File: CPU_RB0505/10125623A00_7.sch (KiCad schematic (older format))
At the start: 71 parts, among them IC20 SN74LVC1G07DBVT, IC6 SN74LVC1G07DBVT, J1 ZIF-52610-2290, J17 FH_40BR, J3 , J6 87606-408, J7 26BR-HE10, T1 2N7002, T16 IRLML5103, T2 2N7002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

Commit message: Renumbered J1's symbol to match footprint
And updated PCB from schematic
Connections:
- wire segments 350 -> 371
- no-connect marks 46 -> 25

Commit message: fix erc errors, change many pin electrical types
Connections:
- wire segments 371 -> 372
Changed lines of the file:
@@
 Text HLabel 8400 4350 0    50   Output ~ 0
 RX-UART-ST
-Text Label 8400 4550 2    50   ~ 0
-LED-PRESENCE-DC
 Text Label 3225 5025 0    56   ~ 0
 LED-PRESENCE-DC
@@
 U 1 1 7D94D0D3
 P 2275 10075
+AR Path="/7D94D0D3" Ref="J3"  Part="1"
+AR Path="/5E926050/7D94D0D3" Ref="J3"  Part="1"
 F 0 "J3" H 2200 9975 59  0000 L BNN
 F 1 " " H 2200 9887 59  0000 L BNN
@@
 	6450 10325 6750 10325
 Wire Wire Line
-	7350 9875 7350 9550
+	7350 9875 7350 9700
 Wire Wire Line
 	7050 9800 7050 9875
@@
 Wire Wire Line
 	2800 5625 3000 5625
-Wire Bus Line
-	12600 2775 14225 2775
-Wire Bus Line
-	11400 3025 14200 3025
 Connection ~ 3000 2025
 Connection ~ 3000 2225
@@
 Connection ~ 3000 5625
 Connection ~ 3000 5825
+$Comp
+L power:PWR_FLAG #FLG0102
+U 1 1 5EB97020
+P 15050 4150
+F 0 "#FLG0102" H 15050 4225 50  0001 C CNN
+F 1 "PWR_FLAG" V 15050 4278 50  0000 L CNN
+F 2 "" H 15050 4150 50  0001 C CNN
+F 3 "~" H 15050 4150 50  0001 C CNN
+	1    15050 4150
+	0    1    1    0
+$EndComp
+Connection ~ 15050 4150
+Text Label 8400 4550 2    50   ~ 0
+LED-PRESENCE-DC
+Wire Bus Line
+	12600 2775 14225 2775
+Wire Bus Line
+	11400 3025 14200 3025
+$Comp
+L power:PWR_FLAG #FLG0110
+U 1 1 600678A7
+P 7325 7475
+F 0 "#FLG0110" H 7325 7550 50  0001 C CNN
+F 1 "PWR_FLAG" V 7325 7603 50  0000 L CNN
+F 2 "" H 7325 7475 50  0001 C CNN
+F 3 "~" H 7325 7475 50  0001 C CNN
+	1    7325 7475
+	0    1    1    0
+$EndComp
+Connection ~ 7325 7475
+$Comp
+L power:PWR_FLAG #FLG0111
+U 1 1 60083738
+P 7350 9700
+F 0 "#FLG0111" H 7350 9775 50  0001 C CNN
+F 1 "PWR_FLAG" V 7350 9828 50  0000 L CNN
+F 2 "" H 7350 9700 50  0001 C CNN
+F 3 "~" H 7350 9700 50  0001 C CNN
+	1    7350 9700
+	0    1    1    0
+$EndComp
+Connection ~ 7350 9700
+Wire Wire Line
+	7350 9700 7350 9550
 $EndSCHEMATC

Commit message: CPU schematic updated to Kicad resistor and cap symbols
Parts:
- C19, C31, C32, C34: symbol cpu-board:TANTALB -> Flipped_Devices:CP_Small
- C35: symbol cpu-board:C0805 -> Flipped_Devices:C_Small
- C87: symbol cpu-board:C0603 -> Flipped_Devices:C_Small
- L5, R12, R13, R20, R21, R24, R25, R26, R27, R30, R32, R47, R7: symbol cpu-board:R0805 -> Flipped_Devices:R
- R16, R22, R23, R31: symbol cpu-board:R1206 -> Flipped_Devices:R
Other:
- moved on the sheet: C17, C18, C41, C52, C55, IC20, IC6, J1, J3, J6, J7, JP1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

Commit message: CPU board diode and transistor symbols changed to Kicad symbols
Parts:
- L1, L16, L18, L3, L35, L36, L38, L39, L4, L40, L41, L42, L43, L44, L45, L46, L47, L48, L49, L50, L51, L52, L53, L6: symbol cpu-board:74279263 -> Flipped_Devices:L
- L61, L8: symbol cpu-board:7427504 -> Flipped_Devices:L
- T1, T2, T4, T5: symbol cpu-board:IRLML2803 -> Flipped_Devices:Q_NMOS_GSD
- T16: symbol cpu-board:IRLML5103 -> Flipped_Devices:Q_PMOS_GSD
- T8, T9: symbol cpu-board:IRLML2803@2 -> Flipped_Devices:Q_NMOS_GSD

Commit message: ran renameSchSyms.py
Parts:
- C19: symbol Flipped_Devices:CP_Small -> Capacitor:C_47uF_10V_10%
- C31, C32, C34: symbol Flipped_Devices:CP_Small -> Capacitor:C_1uF_35V_10%
- C87: symbol Flipped_Devices:C_Small -> Capacitor:C0402_100nF_16V_10%
- IC20: symbol cpu-board:LVC1G07DBVT -> IC:LVC1G07DBVT
- J1: symbol cpu-board:ZIF-52610-2290 -> Connector:ZIF-52610-2290
- J17: symbol cpu-board:FH_40BR -> Connector:FH_40BR
- J3: symbol cpu-board:B12B-ZR -> Connector:B12B-ZR
- J7: symbol cpu-board:26BR-HE10 -> Connector:26BR-HE10
- JP1: symbol cpu-board:JUMP_0U -> Jumper:JUMP_0U
- L1, L16, L18, L3, L35, L4, L42, L43, L44, L45, L46, L47, L48, L49, L50, L51, L52, L53, L6: symbol Flipped_Devices:L -> Inductor:L_10022907
- L5: symbol Flipped_Devices:R -> Inductor:R_470R_5%
- L61, L8: symbol Flipped_Devices:L -> Inductor:L_10022911
- R12, R20, R21, R24, R26, R7: symbol Flipped_Devices:R -> Resistor:R_100k_5%
- R13, R25, R27: symbol Flipped_Devices:R -> Resistor:R0805_620R_5%
- R16: symbol Flipped_Devices:R -> Resistor:R0805_150R_5%
- R22, R23, R31: symbol Flipped_Devices:R -> Resistor:R0805_180R_5%
- R32: symbol Flipped_Devices:R -> Resistor:R0603_10k_5%
- T1, T2, T4, T5, T8, T9: symbol Flipped_Devices:Q_NMOS_GSD -> Transistor:Q_NMOS_GSD_10097274
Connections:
- net at IC20.5 (VCC), L42.2, R47.2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: no longer C87.2
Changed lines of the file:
@@
 SCLK-SPI-0
 $Comp
-L Flipped_Devices:R R13
+L Resistor:R0805_620R_5% R13
 U 1 1 486842E0
 P 3350 4000
@@
 $EndComp
 $Comp
-L Flipped_Devices:R R16
+L Resistor:R0805_150R_5% R16
 U 1 1 BF9499E8
 P 3350 3600
@@
 $EndComp
 $Comp
-L Flipped_Devices:Q_NMOS_GSD T4
+L Transistor:Q_NMOS_GSD_10097274 T4
 U 1 1 4AEDAEDD
 P 5700 3000
@@
 $EndComp
 $Comp
-L Flipped_Devices:R R20
+L Resistor:R_100k_5% R20
 U 1 1 9FEA229A
 P 5900 3200
@@
 $EndComp
 $Comp
-L Flipped_Devices:R R21
+L Resistor:R_100k_5% R21
 U 1 1 F84F2443
 P 6150 4250
@@
 $EndComp
 $Comp
-L Flipped_Devices:Q_NMOS_GSD T8
+L Transistor:Q_NMOS_GSD_10097274 T8
 U 1 1 39E804CC
 P 5200 4550
@@
 $EndComp
 $Comp
-L Flipped_Devices:R R24
+L Resistor:R_100k_5% R24
 U 1 1 84932BAC
 P 5350 4750
@@
 $EndComp
 $Comp
-L Flipped_Devices:R R25
+L Resistor:R0805_620R_5% R25
 U 1 1 D4C34F44
 P 3350 3400
@@
 $EndComp
 $Comp
-L Flipped_Devices:Q_NMOS_GSD T9
+L Transistor:Q_NMOS_GSD_10097274 T9
 U 1 1 7B8E4CC8
 P 5200 3500
@@
 $EndComp
 $Comp
-L Flipped_Devices:R R26
+L Resistor:R_100k_5% R26
 U 1 1 AD264776
 P 5400 3700
@@
 $EndComp
 $Comp
-L Flipped_Devices:CP_Small C31
+L Capacitor:C_1uF_35V_10% C31
 U 1 1 0C4556A5
 P 10600 2800
@@
 $EndComp
 $Comp
-L Flipped_Devices:CP_Small C32
+L Capacitor:C_1uF_35V_10% C32
 U 1 1 FD532AD7
 P 10600 1300
@@
 $EndComp
 $Comp
-L Flipped_Devices:R R32
+L Resistor:R0603_10k_5% R32
 U 1 1 2A092FBD
 P 7750 7900
@@
 $EndComp
 $Comp
-L Flipped_Devices:R R7
+L Resistor:R_100k_5% R7
 U 1 1 184A3E63
 P 4800 5350
@@
 $EndComp
 $Comp
-L Flipped_Devices:Q_NMOS_GSD T2
+L Transistor:Q_NMOS_GSD_10097274 T2
 U 1 1 4E5B5821
 P 5750 2100
@@
 $EndComp
 $Comp
-L Flipped_Devices:R R12
+L Resistor:R_100k_5% R12
 U 1 1 0C5252B0
 P 5950 2300
@@
 $EndComp
 $Comp
-L Flipped_Devices:R R22
+L Resistor:R0805_180R_5% R22
 U 1 1 50E1B837
 P 3350 4800
@@
 $EndComp
 $Comp
-L Flipped_Devices:R R23
+L Resistor:R0805_180R_5% R23
 U 1 1 AE8C3E2E
 P 3350 3000
@@
 $EndComp
 $Comp
-L Flipped_Devices:L L16
+L Inductor:L_10022907 L16
 U 1 1 3E1ECFE2
 P 8650 4350
@@
 $EndComp
 $Comp
-L Flipped_Devices:L L18
+L Inductor:L_10022907 L18
 U 1 1 C853FF9C
 P 8650 4550
@@
 $EndComp
 $Comp
-L Flipped_Devices:L L1
+L Inductor:L_10022907 L1
 U 1 1 63106439
 P 8650 4650
@@
 $EndComp
 $Comp
-L Flipped_Devices:L L3
+L Inductor:L_10022907 L3
 U 1 1 5E88F353
 P 8650 4750
@@
 $EndComp
 $Comp
-L Flipped_Devices:L L4
+L Inductor:L_10022907 L4
 U 1 1 AC576572
 P 8650 4850
@@
 $EndComp
 $Comp
-L Flipped_Devices:L L6
+L Inductor:L_10022907 L6
 U 1 1 76104BF1
 P 8650 5050
@@
 $EndComp
 $Comp
-L Flipped_Devices:L L43
+L Inductor:L_10022907 L43
 U 1 1 B8451C4A
 P 14550 4950
@@
 $EndComp
 $Comp
-L Flipped_Devices:L L44
+L Inductor:L_10022907 L44
 U 1 1 C8827D52
 P 14550 4850
@@
 $EndComp
 $Comp
-L Flipped_Devices:L L45
+L Inductor:L_10022907 L45
 U 1 1 27E57B0C
 P 14550 4750
@@
 $EndComp
 $Comp
-L Flipped_Devices:L L47
+L Inductor:L_10022907 L47
 U 1 1 58FFAA19
 P 14550 4550
@@
 $EndComp
 $Comp
-L Flipped_Devices:L L48
+L Inductor:L_10022907 L48
 U 1 1 7A9C51D5
 P 14550 4450
@@
 $EndComp
 $Comp
-L Flipped_Devices:L L49
+L Inductor:L_10022907 L49
 U 1 1 B59E7860
 P 14550 4350
@@
 $EndComp
 $Comp
-L Flipped_Devices:L L50
+L Inductor:L_10022907 L50
 U 1 1 39D83C75
 P 14550 4250
@@
 $EndComp
 $Comp
-L Flipped_Devices:L L61
+L Inductor:L_10022911 L61
 U 1 1 D3E71165
 P 14550 4150
@@
 $EndComp
 $Comp
-L cpu-board:26BR-HE10 J7
+L Connector:26BR-HE10 J7
 U 1 1 916830BC
 P 11250 4650
@@
 $EndComp
 $Comp
-L Flipped_Devices:L L8
+L Inductor:L_10022911 L8
 U 1 1 8A653321
 P 14550 5150
@@
 $EndComp
 $Comp
-L Flipped_Devices:CP_Small C19
+L Capacitor:C_47uF_10V_10% C19
 U 1 1 9CA42FFB
 P 3200 8450
@@
 $EndComp
 $Comp
-L cpu-board:B12B-ZR J3
+L Connector:B12B-ZR J3
 U 1 1 7D94D0D3
 P 2250 10100
@@
 $EndComp
 $Comp
-L Flipped_Devices:L L35
+L Inductor:L_10022907 L35
 U 1 1 3EE6CC19
 P 4950 8200
@@
 $EndComp
 $Comp
-L Flipped_Devices:L L42
+L Inductor:L_10022907 L42
 U 1 1 68BA90A5
 P 4950 7450
@@
 $EndComp
 $Comp
-L Flipped_Devices:C_Small C87
+L Capacitor:C0402_100nF_16V_10% C87
 U 1 1 DE7D17FD
 P 5950 7775
@@
 $EndComp
 $Comp
-L cpu-board:JUMP_0U JP1
+L Jumper:JUMP_0U JP1
 U 1 1 0B60073D
 P 4700 10250
@@
 $EndComp
 $Comp
-L Flipped_Devices:L L46
+L Inductor:L_10022907 L46
 U 1 1 17AB747C
 P 14550 4650
@@
 $EndComp
 $Comp
-L Flipped_Devices:L L51
+L Inductor:L_10022907 L51
 U 1 1 49C38A30
 P 8650 4250
@@
 $EndComp
 $Comp
-L Flipped_Devices:L L52
+L Inductor:L_10022907 L52
 U 1 1 5D3B4218
 P 8650 4450
@@
 $EndComp
 $Comp
-L Flipped_Devices:L L53
+L Inductor:L_10022907 L53
 U 1 1 983C8A5F
 P 14550 5050
@@
 $EndComp
 $Comp
-L Flipped_Devices:R L5
+L Inductor:R_470R_5% L5
 U 1 1 E13C76CE
 P 8650 4950
@@
 	3000 5800 3100 5800
 $Comp
-L Flipped_Devices:R R31
+L Resistor:R0805_180R_5% R31
 U 1 1 63ABC06C
 P 3350 5200
@@
 NoConn ~ 3000 2800
 $Comp
-L Flipped_Devices:R R27
+L Resistor:R0805_620R_5% R27
 U 1 1 4A61E0AF
 P 3350 4200
@@
 $EndComp
 $Comp
-L Flipped_Devices:Q_NMOS_GSD T1
+L Transistor:Q_NMOS_GSD_10097274 T1
 U 1 1 C746FFC6
 P 4600 5150
@@
 Connection ~ 7750 8200
 $Comp
-L cpu-board:LVC1G07DBVT IC20
+L IC:LVC1G07DBVT IC20
 U 1 1 7427DFBC
 P 7050 8200
@@
 	14700 5050 14850 5050
 $Comp
-L cpu-board:FH_40BR J17
+L Connector:FH_40BR J17
 U 1 1 E8FF25C4
 P 12600 2150
@@
 $EndComp
 $Comp
-L Flipped_Devices:CP_Small C34
+L Capacitor:C_1uF_35V_10% C34
 U 1 1 555B33A9
 P 14375 1300
@@
 	3000 3800 3300 3800
 $Comp
-L cpu-board:ZIF-52610-2290 J1
+L Connector:ZIF-52610-2290 J1
 U 1 1 449C7C68
 P 2800 5900
@@
 	5850 3850 5850 3700
 $Comp
-L Flipped_Devices:Q_NMOS_GSD T5
+L Transistor:Q_NMOS_GSD_10097274 T5
 U 1 1 58A3FA22
 P 5950 4050

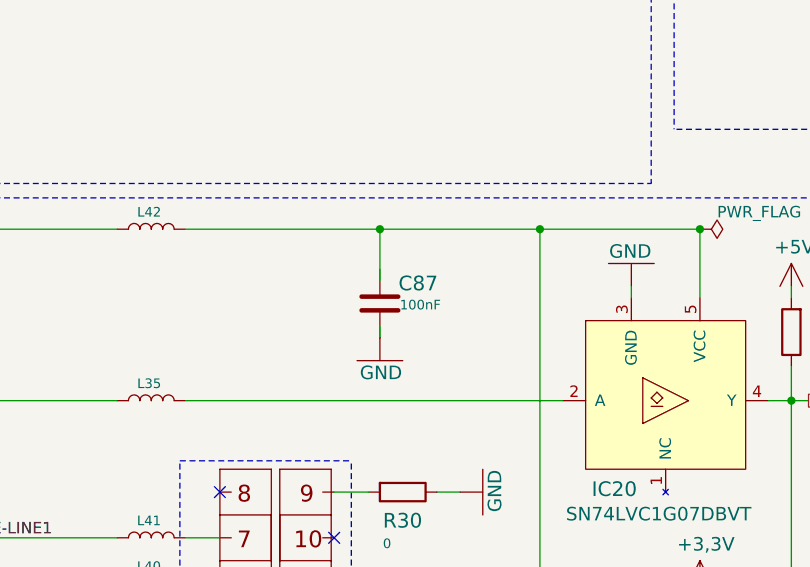
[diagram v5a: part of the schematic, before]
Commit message: CPU board passed ERC and matches Update PCB report
Schematic needs cleanup!
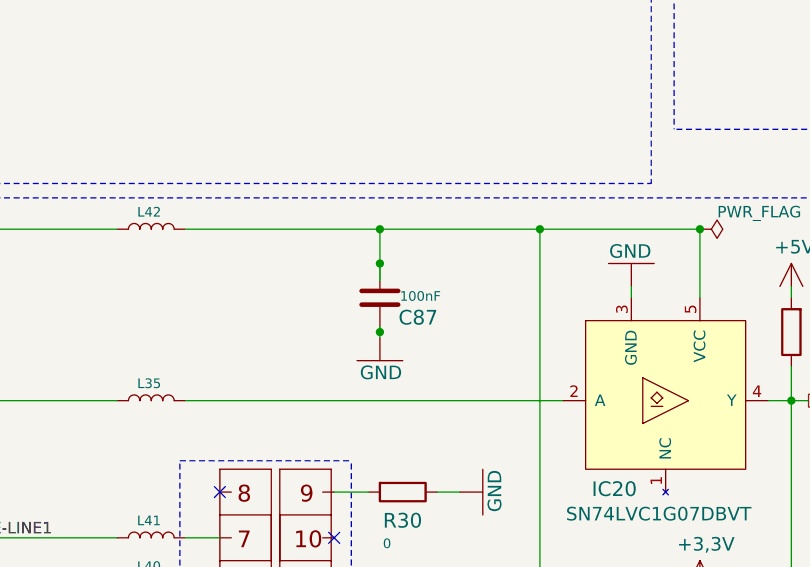
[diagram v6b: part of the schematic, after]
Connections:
- net at IC20.5 (VCC), L42.2, R47.2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: now also C87.2
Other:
- moved on the sheet: C87
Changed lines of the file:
@@
 L Capacitor:C0402_100nF_16V_10% C87
 U 1 1 DE7D17FD
-P 5950 7775
-F 0 "C87" H 6031 7825 64  0000 L BNN
-F 1 "100nF" H 6037 7744 42  0000 L BNN
-F 2 "AllModules:C0402_1" H 5950 7775 50  0001 C CNN
-F 3 "" H 5950 7775 50  0001 C CNN
-	1    5950 7775
-	1    0    0    -1
+P 5950 7750
+F 0 "C87" H 6031 7800 64  0000 L BNN
+F 1 "100nF" H 6037 7719 42  0000 L BNN
+F 2 "AllModules:C0402_1" H 5950 7750 50  0001 C CNN
+F 3 "" H 5950 7750 50  0001 C CNN
+	1    5950 7750
+	1    0    0    1
 $EndComp
 $Comp
@@
 	5950 7450 6650 7450
 Wire Wire Line
-	5950 7450 5950 7675
-Wire Wire Line
-	5950 7925 5950 7875
+	5950 7450 5950 7600
+Wire Wire Line
+	5950 7925 5950 7900
 Connection ~ 6650 7450
 Wire Wire Line
@@
 	3850 7450 3850 7800
 Connection ~ 7350 7450
+Connection ~ 5950 7600
+Connection ~ 5950 7900
+Wire Wire Line
+	5950 7900 5950 7875
+Wire Wire Line
+	5950 7600 5950 7675
 Wire Bus Line
 	12600 2775 14225 2775

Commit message: Symbols and links update: sch page 7 and global lib
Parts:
- C111, C17, C18, C41, C52, C55, C58: symbol cpu-board:RESEAU_4C -> Capacitor:C0612_47pF_50V_10%
- C35: value 100nF -> DNP; symbol Flipped_Devices:C_Small -> Capacitor:C0402_100nF_16V_10%; Item Number (none) -> 10022607
- C87: Item Number (none) -> 10022607
- IC6: value SN74LVC1G07DBVT -> DNP; symbol cpu-board:LVC1G07DBVT -> IC:LVC1G07DBVT; Item Number (none) -> 10022964; Manufacturer (none) -> TEXAS INSTRUMENTS_RMS1; Manufacturer_No (none) -> SN74LVC1G07DBVT
- J6: value 87606-408 -> DNP; symbol cpu-board:87606-408 -> Connector:87606-408; Manufacturer_No (none) -> 87606-408
- JP1: Manufacturer4 ASJ -> (none); Manufacturer5 KAMAYA (049580) -> (none); Manufacturer_Desc4 THICK FILM CHIP RESISTOR -> (none); Manufacturer_Desc5 JUMPER -> (none); Manufacturer_No4 CR16000ZL -> (none); Manufacturer_No5 RMC1/16JPTP -> (none)
- L36, L38, L39, L40, L41: value Ferrite 200mA -> DNP; Item Number (none) -> 10022907
- R12, R20, R21, R24, R26, R7: Manufacturer4 PANASONIC_RMS1 -> (none); Manufacturer_Desc4 THICK FILM CHIP RESISTOR -> (none); Manufacturer_No4 ERJ3GEYJ104V -> (none)
- R30: value 0 -> DNP; symbol Flipped_Devices:R -> Resistor:R0603_0R_5%; Item Number (none) -> 10023185
- R32: Manufacturer4 ASJ -> (none); Manufacturer5 YAGEO_RMS1 -> (none); Manufacturer_Desc4 THICK FILM CHIP RESISTOR -> (none); Manufacturer_Desc5 RESISTOR, METAL GLAZE/THICK FILM, 0.1 W, 5 %, 100 PPM, 1000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 -> (none); Manufacturer_No4 CR16-103JL -> (none); Manufacturer_No5 RC0603JR-0710KL -> (none)
- R47: value 10k -> DNP; symbol Flipped_Devices:R -> Resistor:R0603_10k_5%; Item Number (none) -> 10097266
- T16: value IRLML5103 -> DNP; symbol Flipped_Devices:Q_PMOS_GSD -> Transistor:Q_PMOS_GSD_10022933; Item Number (none) -> 10022933; Manufacturer (none) -> INTERNATIONAL RECTIFIER_RMS1; Manufacturer_No (none) -> IRLML5103
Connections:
- net at C35.1: now also J6.15; no longer J6.16
- net at C35.2: now also J6.16; no longer J6.15
